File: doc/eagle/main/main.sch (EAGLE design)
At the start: 27 parts, among them U1 168A-PU

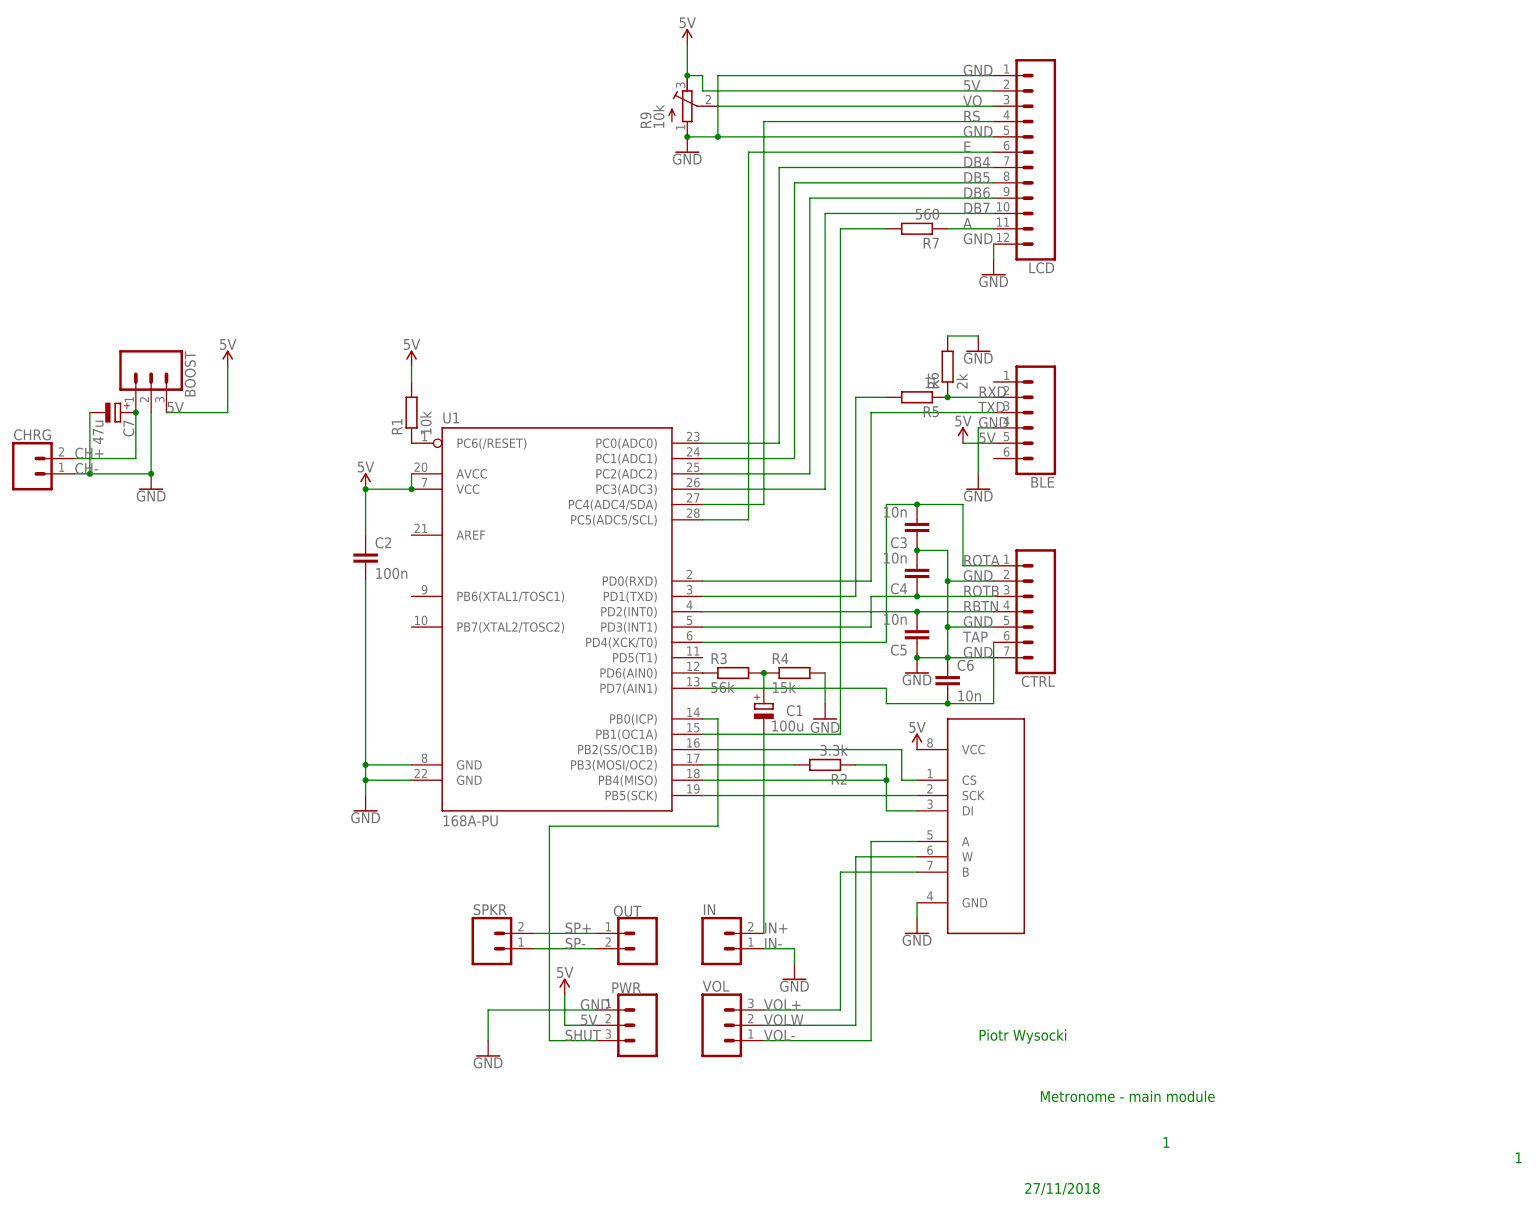
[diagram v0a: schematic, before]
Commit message: Eagle files, eeprom empty *.h and *.c
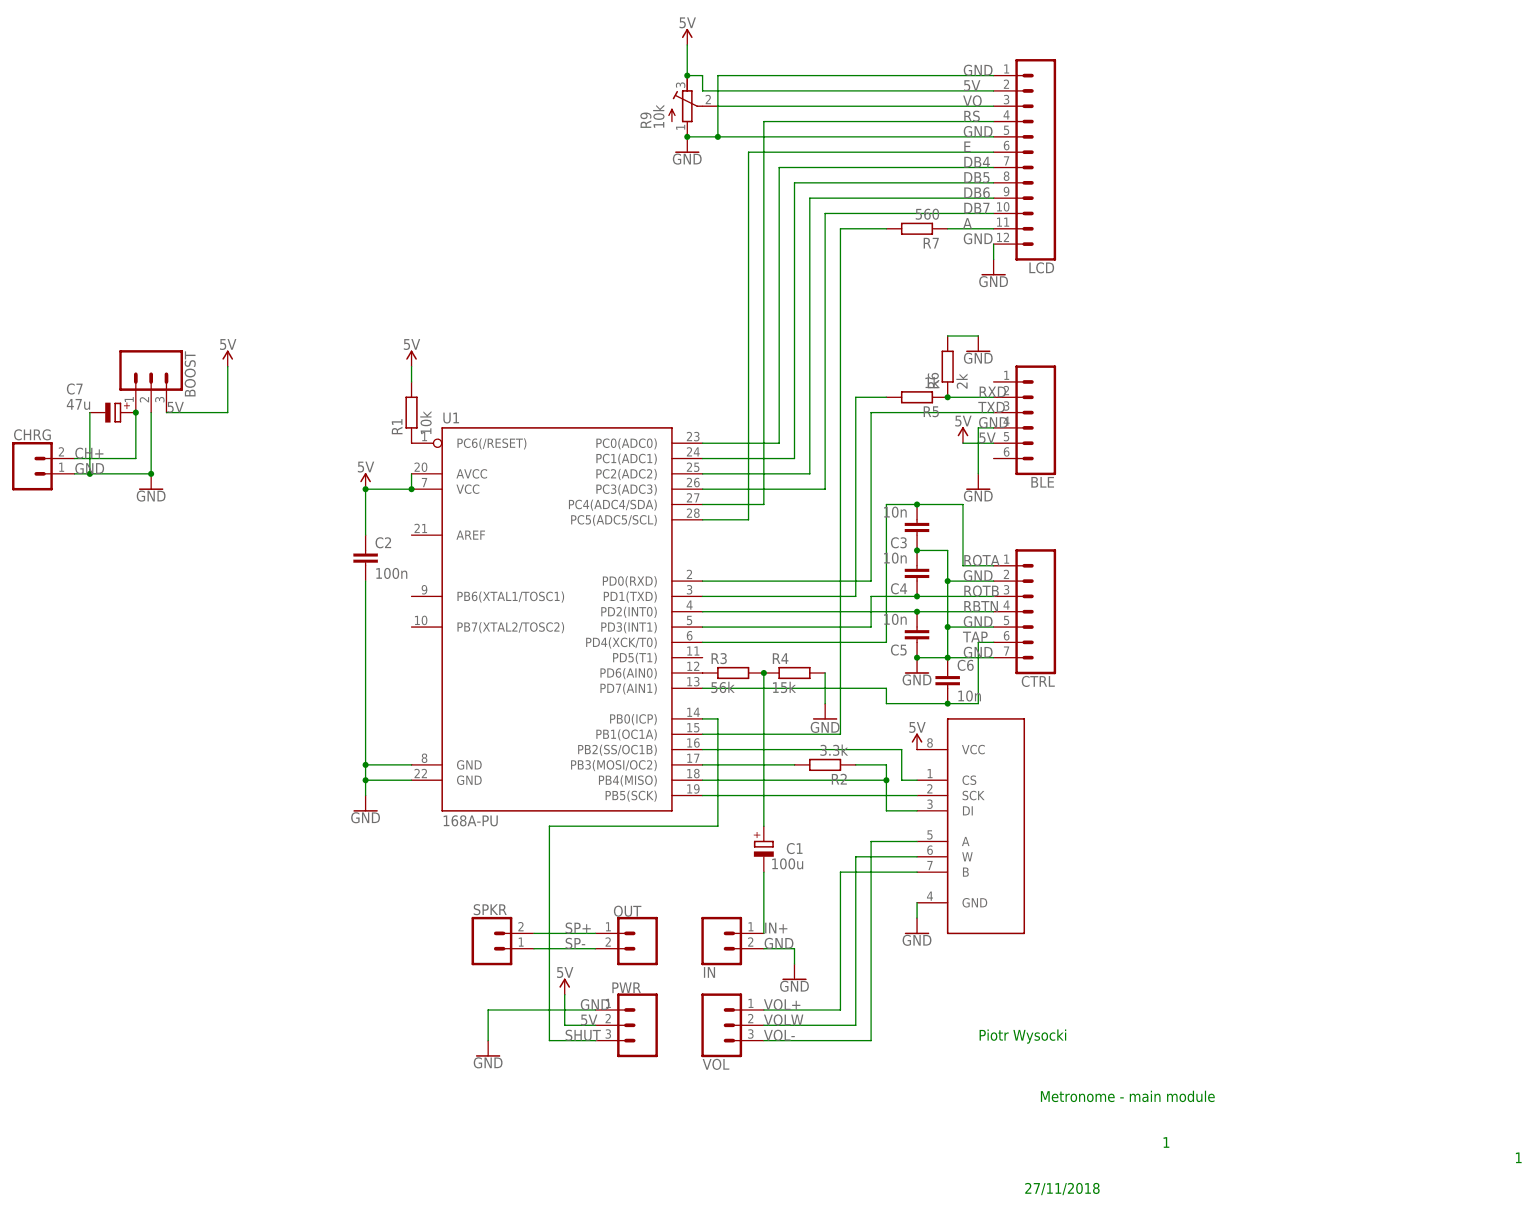
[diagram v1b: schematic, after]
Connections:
- removed net CH-: BOOST.2, C7.-, CHRG.1
- removed net IN-: IN.1
- net GND: now also BOOST.2, C7.-, CHRG.1, IN.2
- net IN+: now also IN.1; no longer IN.2
- net VOL+: now also VOL.1; no longer VOL.3
- net VOL-: now also VOL.3; no longer VOL.1
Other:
- moved on the sheet: C1, IN, VOL

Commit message: Storing metronome params in EEPROM after user inactivity, Eagle files + PDF exports
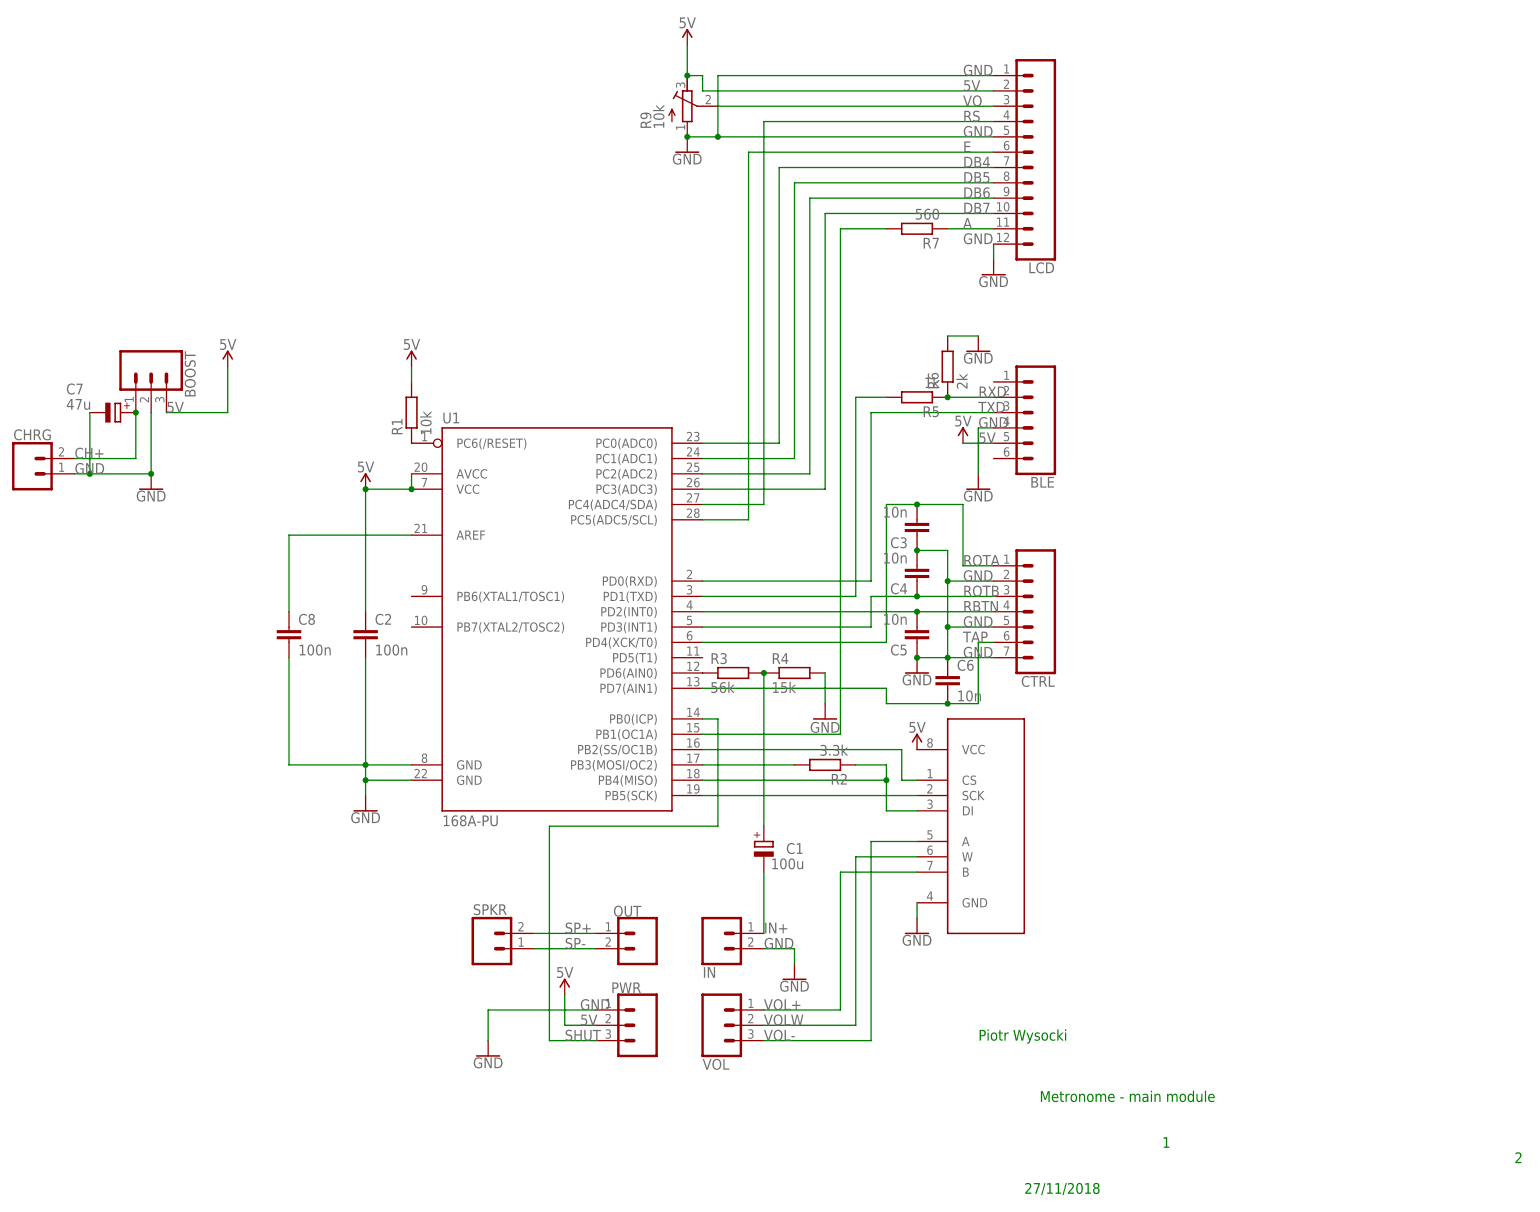
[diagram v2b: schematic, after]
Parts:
- added C8: 100n, rcl:C-EU025-024X044
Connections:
- new net N$6: C8.1, U1.AREF
- net GND: now also C8.2
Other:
- note added: "2"
- moved on the sheet: C2
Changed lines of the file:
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@@
 <?xml version="1.0" encoding="utf-8"?>
 <!DOCTYPE eagle SYSTEM "eagle.dtd">
-<eagle version="7.7.0">
+<eagle version="9.2.2">
 <drawing>
 <settings>
 <setting alwaysvectorfont="no"/>
+<setting keepoldvectorfont="yes"/>
 <setting verticaltext="up"/>
 </settings>
@@
 <part name="FRAME1" library="frames" deviceset="FRAME_A_L" device=""/>
 <part name="R9" library="rcl" deviceset="R-TRIMM" device="3296W" value="10k"/>
+<part name="C8" library="rcl" deviceset="C-EU" device="025-024X044" value="100n"/>
 </parts>
 <sheets>
@@
 <text x="144.78" y="-45.72" size="1.778" layer="91">1</text>
 <text x="121.92" y="-53.34" size="1.778" layer="91">27/11/2018</text>
-<text x="203.2" y="-48.26" size="1.778" layer="91">1</text>
+<text x="203.2" y="-48.26" size="1.778" layer="91">2</text>
 </plain>
 <instances>
@@
 <attribute name="VALUE" x="79.883" y="0.4826" size="1.778" layer="96"/>
 </instance>
-<instance part="C2" gate="G$1" x="12.7" y="53.34" smashed="yes">
-<attribute name="NAME" x="14.224" y="53.721" size="1.778" layer="95"/>
-<attribute name="VALUE" x="14.224" y="48.641" size="1.778" layer="96"/>
+<instance part="C2" gate="G$1" x="12.7" y="40.64" smashed="yes">
+<attribute name="NAME" x="14.224" y="41.021" size="1.778" layer="95"/>
+<attribute name="VALUE" x="14.224" y="35.941" size="1.778" layer="96"/>
 </instance>
 <instance part="C3" gate="G$1" x="104.14" y="55.88" smashed="yes" rot="R180">
@@
 <attribute name="NAME" x="60.071" y="123.19" size="1.778" layer="95" rot="R90"/>
 <attribute name="VALUE" x="62.23" y="123.19" size="1.778" layer="96" rot="R90"/>
+</instance>
+<instance part="C8" gate="G$1" x="0" y="40.64" smashed="yes">
+<attribute name="NAME" x="1.524" y="41.021" size="1.778" layer="95"/>
+<attribute name="VALUE" x="1.524" y="35.941" size="1.778" layer="96"/>
 </instance>
 </instances>
@@
 <segment>
 <pinref part="C2" gate="G$1" pin="2"/>
-<wire x1="12.7" y1="48.26" x2="12.7" y2="17.78" width="0.1524" layer="91"/>
+<wire x1="12.7" y1="35.56" x2="12.7" y2="17.78" width="0.1524" layer="91"/>
 <pinref part="U1" gate="G$1" pin="GND@2"/>
 <wire x1="12.7" y1="17.78" x2="12.7" y2="15.24" width="0.1524" layer="91"/>
@@
 <wire x1="12.7" y1="15.24" x2="12.7" y2="12.7" width="0.1524" layer="91"/>
 <junction x="12.7" y="15.24"/>
+<pinref part="C8" gate="G$1" pin="2"/>
+<wire x1="0" y1="35.56" x2="0" y2="17.78" width="0.1524" layer="91"/>
+<wire x1="0" y1="17.78" x2="12.7" y2="17.78" width="0.1524" layer="91"/>
 </segment>
 <segment>
@@
 <pinref part="C2" gate="G$1" pin="1"/>
 <wire x1="12.7" y1="63.5" x2="20.32" y2="63.5" width="0.1524" layer="91"/>
-<wire x1="12.7" y1="55.88" x2="12.7" y2="63.5" width="0.1524" layer="91"/>
+<wire x1="12.7" y1="43.18" x2="12.7" y2="63.5" width="0.1524" layer="91"/>
 <junction x="12.7" y="63.5"/>
 <pinref part="U1" gate="G$1" pin="AVCC"/>
@@
 </segment>
 </net>
+<net name="N$6" class="0">
+<segment>
+<pinref part="C8" gate="G$1" pin="1"/>
+<wire x1="0" y1="43.18" x2="0" y2="55.88" width="0.1524" layer="91"/>
+<pinref part="U1" gate="G$1" pin="AREF"/>
+<wire x1="0" y1="55.88" x2="20.32" y2="55.88" width="0.1524" layer="91"/>
+</segment>
+</net>
